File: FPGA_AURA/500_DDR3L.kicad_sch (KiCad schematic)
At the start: 1 part, among them U500 MT41K128M16JT-125_IT_K

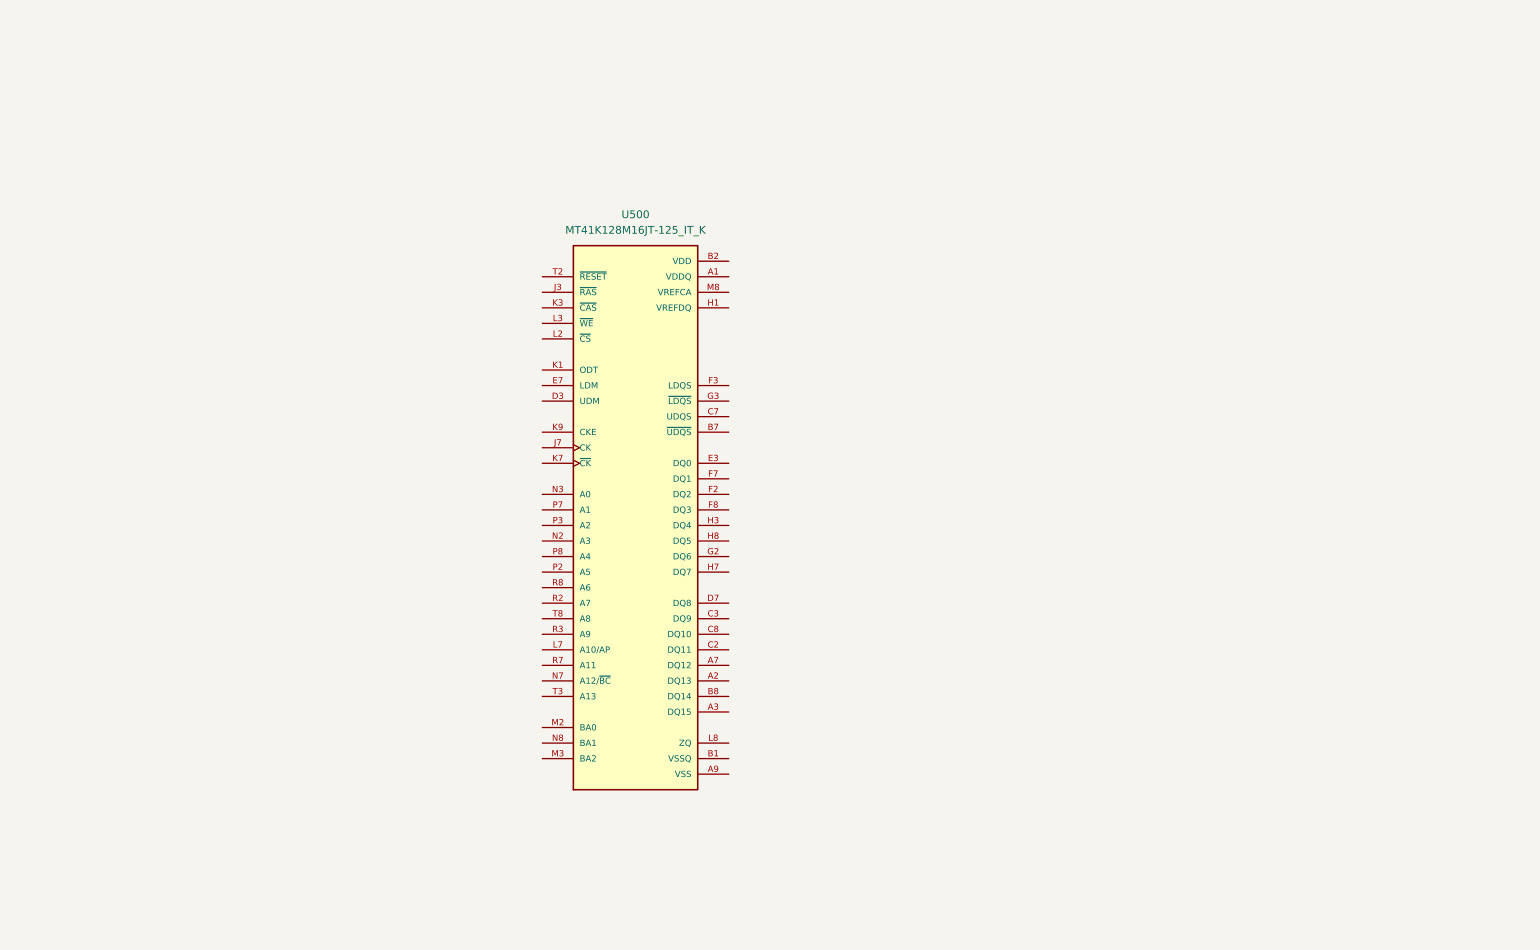
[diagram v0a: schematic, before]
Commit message: Added USB power schottky and started DDR3L
Transferring from laptop to PC to decide DDR3 pins.
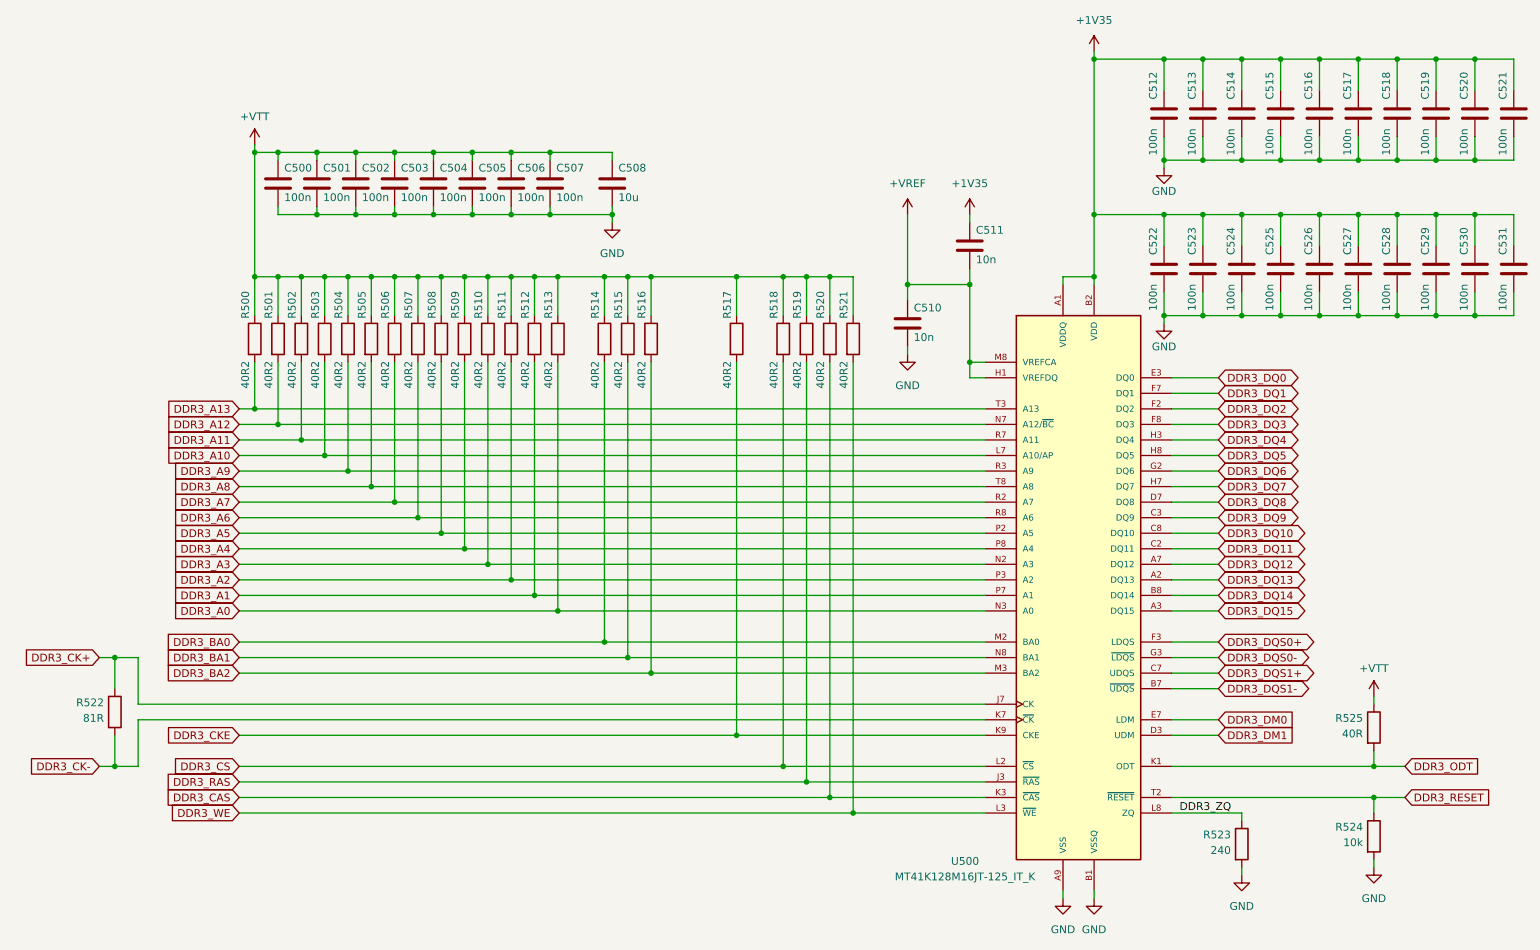
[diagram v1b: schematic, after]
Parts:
- added C500, C501, C502, C503, C504, C505, C506, C507, C512, C513, C514, C515, C516, C517, C518, C519, C520, C521, C522, C523, C524, C525, C526, C527, C528, C529, C530, C531: 100n, Capacitor_SMD:C_0402_1005Metric, symbol Device:C
- added C508: 10u, Capacitor_SMD:C_0402_1005Metric, symbol Device:C
- added C510, C511: 10n, Capacitor_SMD:C_0402_1005Metric, symbol Device:C
- added R500, R501, R502, R503, R504, R505, R506, R507, R508, R509, R510, R511, R512, R513, R514, R515, R516, R517, R518, R519, R520, R521: 40R2, Resistor_SMD:R_0402_1005Metric, symbol Device:R
- added R522: 81R, Resistor_SMD:R_0402_1005Metric, symbol Device:R
- added R523: 240, Resistor_SMD:R_0402_1005Metric, symbol Device:R
- added R524: 10k, Resistor_SMD:R_0402_1005Metric, symbol Device:R
- added R525: 40R, Resistor_SMD:R_0402_1005Metric, symbol Device:R
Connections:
- net VDDQ is gone; now on net +1V35: U500.A1 (VDDQ), U500.A8 (VDDQ), U500.C1 (VDDQ), U500.C9 (VDDQ), U500.D2 (VDDQ), U500.E9 (VDDQ), U500.F1 (VDDQ), U500.H2 (VDDQ), U500.H9 (VDDQ)
- net DDR3_DQ13: now reaches U500.A2 (DQ13)
- net DDR3_DQ15: now reaches U500.A3 (DQ15)
- net DDR3_DQ12: now reaches U500.A7 (DQ12)
- net GND: now reaches U500.A9 (VSS), U500.B3 (VSS), U500.E1 (VSS), U500.G8 (VSS), U500.J2 (VSS), U500.J8 (VSS), U500.M1 (VSS), U500.M9 (VSS), U500.P1 (VSS), U500.P9 (VSS), U500.T1 (VSS), U500.T9 (VSS)
- net GND: now also U500.B1 (VSSQ), U500.B9 (VSSQ), U500.D1 (VSSQ), U500.D8 (VSSQ), U500.E2 (VSSQ), U500.E8 (VSSQ), U500.F9 (VSSQ), U500.G1 (VSSQ), U500.G9 (VSSQ), C500.2, C501.2, C502.2, C503.2, C504.2, C505.2, C506.2, C507.2, C508.2, C510.2, C512.2, C513.2, C514.2, C515.2, C516.2, C517.2, C518.2, C519.2, C520.2, C521.2, C522.2, C523.2, C524.2, C525.2, C526.2, C527.2, C528.2, C529.2, C530.2, C531.2, R523.2, R524.2
- net DDR3_DQS1-: now reaches U500.B7 (~{UDQS})
- net DDR3_DQ14: now reaches U500.B8 (DQ14)
- net DDR3_DQ11: now reaches U500.C2 (DQ11)
- net DDR3_DQ9: now reaches U500.C3 (DQ9)
- net DDR3_DQS1+: now reaches U500.C7 (UDQS)
- net DDR3_DQ10: now reaches U500.C8 (DQ10)
- net DDR3_DM1: now reaches U500.D3 (UDM)
- net DDR3_DQ8: now reaches U500.D7 (DQ8)
- net DDR3_DQ0: now reaches U500.E3 (DQ0)
- net DDR3_DM0: now reaches U500.E7 (LDM)
- net DDR3_DQ2: now reaches U500.F2 (DQ2)
- net DDR3_DQS0+: now reaches U500.F3 (LDQS)
- net DDR3_DQ1: now reaches U500.F7 (DQ1)
- net DDR3_DQ3: now reaches U500.F8 (DQ3)
- net DDR3_DQ6: now reaches U500.G2 (DQ6)
- net DDR3_DQS0-: now reaches U500.G3 (~{LDQS})
- net +VREF: now reaches U500.H1 (VREFDQ)
- net +VREF: now also U500.M8 (VREFCA), C510.1, C511.2
- net DDR3_DQ4: now reaches U500.H3 (DQ4)
- net DDR3_DQ7: now reaches U500.H7 (DQ7)
- net DDR3_DQ5: now reaches U500.H8 (DQ5)
- net DDR3_RAS: now reaches U500.J3 (~{RAS})
- net DDR3_RAS: now also R519.2
- net DDR3_CK+: now reaches U500.J7 (CK)
- net DDR3_CK+: now also R522.1
- net DDR3_ODT: now reaches U500.K1 (ODT)
- net DDR3_ODT: now also R525.2
- net DDR3_CAS: now reaches U500.K3 (~{CAS})
- net DDR3_CAS: now also R520.2
- net DDR3_CK-: now reaches U500.K7 (~{CK})
- net DDR3_CK-: now also R522.2
- net DDR3_CKE: now reaches U500.K9 (CKE)
- net DDR3_CKE: now also R517.2
- net DDR3_CS: now reaches U500.L2 (~{CS})
- net DDR3_CS: now also R518.2
- net DDR3_WE: now reaches U500.L3 (~{WE})
- net DDR3_WE: now also R521.2
- net DDR3_A10: now reaches U500.L7 (A10/AP)
- net DDR3_A10: now also R503.2
- net DDR3_ZQ: now reaches U500.L8 (ZQ)
- net DDR3_ZQ: now also R523.1
- net DDR3_BA0: now reaches U500.M2 (BA0)
- net DDR3_BA0: now also R514.2
- net DDR3_BA2: now reaches U500.M3 (BA2)
- net DDR3_BA2: now also R516.2
- net DDR3_A3: now reaches U500.N2 (A3)
- net DDR3_A3: now also R510.2
- net DDR3_A0: now reaches U500.N3 (A0)
- net DDR3_A0: now also R513.2
- net DDR3_A12: now reaches U500.N7 (A12/~{BC})
- net DDR3_A12: now also R501.2
- net DDR3_BA1: now reaches U500.N8 (BA1)
- net DDR3_BA1: now also R515.2
- net DDR3_A5: now reaches U500.P2 (A5)
- net DDR3_A5: now also R508.2
- net DDR3_A2: now reaches U500.P3 (A2)
- net DDR3_A2: now also R511.2
- net DDR3_A1: now reaches U500.P7 (A1)
- net DDR3_A1: now also R512.2
- net DDR3_A4: now reaches U500.P8 (A4)
- net DDR3_A4: now also R509.2
- net DDR3_A7: now reaches U500.R2 (A7)
- net DDR3_A7: now also R506.2
- net DDR3_A9: now reaches U500.R3 (A9)
- net DDR3_A9: now also R504.2
- net DDR3_A11: now reaches U500.R7 (A11)
- net DDR3_A11: now also R502.2
- net DDR3_A6: now reaches U500.R8 (A6)
- net DDR3_A6: now also R507.2
- net DDR3_RESET: now reaches U500.T2 (~{RESET})
- net DDR3_RESET: now also R524.1
- net DDR3_A13: now reaches U500.T3 (A13)
- net DDR3_A13: now also R500.2
- net DDR3_A8: now reaches U500.T8 (A8)
- net DDR3_A8: now also R505.2
- net VDD renamed +1V35
- net +1V35: now also C511.1, C512.1, C513.1, C514.1, C515.1, C516.1, C517.1, C518.1, C519.1, C520.1, C521.1, C522.1, C523.1, C524.1, C525.1, C526.1, C527.1, C528.1, C529.1, C530.1, C531.1
- new net +VTT: C500.1, C501.1, C502.1, C503.1, C504.1, C505.1, C506.1, C507.1, C508.1, R500.1, R501.1, R502.1, R503.1, R504.1, R505.1, R506.1, R507.1, R508.1, R509.1, R510.1, R511.1, R512.1, R513.1, R514.1, R515.1, R516.1, R517.1, R518.1, R519.1, R520.1, R521.1, R525.1
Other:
- moved on the sheet: U500
